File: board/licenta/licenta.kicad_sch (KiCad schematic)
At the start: 57 parts, among them IC1 SAMACSYS_PARTS_NCP186BMX330TAG, IC3 SAMACSYS_PARTS_BMI085, J1 SAMACSYS_PARTS_USB4110-GF-A, J2 SAMACSYS_PARTS_112A-TAAR-R03_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, Q1 ESP32_WROVER_SPARKFUN-DISCRET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, Q2 2N7002, SW1 SW_Push, SW2 SW_Push, SW3 SW_Push, SW6 SW_Push, U2 ESP32_WROVER_SPARKFUN-IC-POWE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, U3 DRV2605LDGS, U4 GC9A01_IPS_display_SPI, U7 ESP32-S3-MINI-1

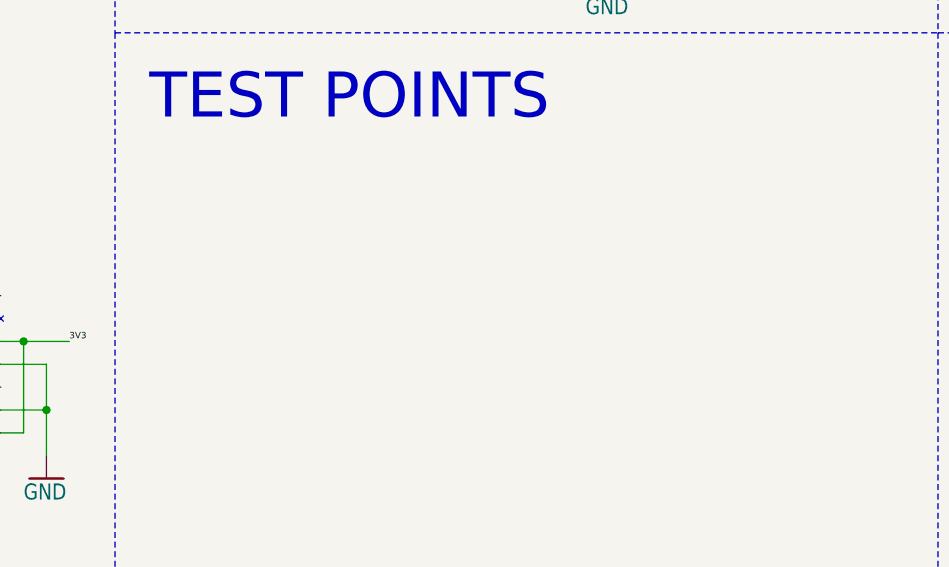
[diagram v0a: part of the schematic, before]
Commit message: Add DRU and minor pads update
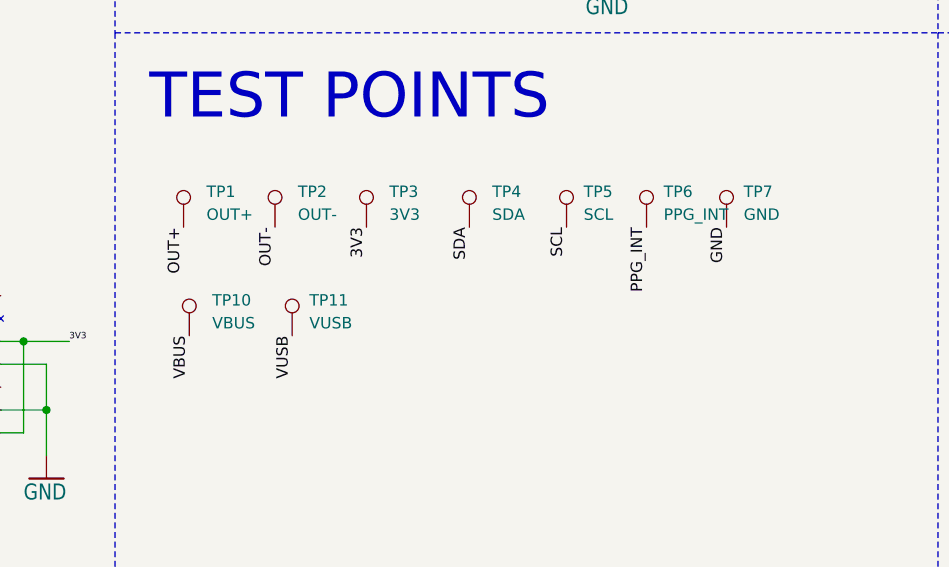
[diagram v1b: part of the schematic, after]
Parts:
- added TP1: OUT+, TestPoint:TestPoint_Pad_D2.0mm, symbol Connector:TestPoint
- added TP10: VBUS, TestPoint:TestPoint_Pad_1.0x1.0mm, symbol Connector:TestPoint
- added TP11: VUSB, TestPoint:TestPoint_Pad_1.0x1.0mm, symbol Connector:TestPoint
- added TP2: OUT-, TestPoint:TestPoint_Pad_D2.0mm, symbol Connector:TestPoint
- added TP3: 3V3, TestPoint:TestPoint_Pad_D2.0mm, symbol Connector:TestPoint
- added TP4: SDA, TestPoint:TestPoint_Pad_D2.0mm, symbol Connector:TestPoint
- added TP5: SCL, TestPoint:TestPoint_Pad_D2.0mm, symbol Connector:TestPoint
- added TP6: PPG_INT, TestPoint:TestPoint_Pad_D2.0mm, symbol Connector:TestPoint
- added TP7: GND, TestPoint:TestPoint_Pad_D2.0mm, symbol Connector:TestPoint
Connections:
- net 3V3: now also TP3.1
- net GND: now also TP7.1
- net OUT+: now also TP1.1
- net OUT-: now also TP2.1
- net PPG_INT: now also TP6.1
- net SCL: now also TP5.1
- net SDA: now also TP4.1
- net VBUS: now also TP10.1
- net VUSB: now also TP11.1

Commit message: Add DRC and start routing
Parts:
- removed TP11: VUSB, TestPoint:TestPoint_Pad_1.0x1.0mm, symbol Connector:TestPoint
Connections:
- net LTR_INT is gone; now on net IMU_INT: U7.15 (GPIO11/TOUCH11/ADC2_CH0/FSPID/FSPIIO5/SUBSPID)
- net DISP_RST: now also U7.20 (GPIO16/U0CTS/ADC2_CH5/XTAL_32K_N); no longer U7.10 (GPIO6/TOUCH6/ADC1_CH5)
- net GND: now also U7.1 (GND), U7.2 (GND), U7.42 (GND), U7.43 (GND), U7.46 (GND), U7.47 (GND), U7.48 (GND), U7.49 (GND), U7.50 (GND), U7.51 (GND), U7.52 (GND), U7.53 (GND), U7.54 (GND), U7.55 (GND), U7.56 (GND), U7.57 (GND), U7.58 (GND), U7.59 (GND), U7.60 (GND), U7.61 (GND), U7.62 (GND), U7.63 (GND), U7.64 (GND), U7.65 (GND)
- net IMU_INT: no longer U7.11 (GPIO7/TOUCH7/ADC1_CH6)
- net SS_SD: now also U7.21 (GPIO17/U1TXD/ADC2_CH6); no longer U7.9 (GPIO5/TOUCH5/ADC1_CH4)
- net TFT_DC: now also U7.22 (GPIO18/U1RXD/ADC2_CH7/CLK_OUT3); no longer U7.6 (GPIO2/TOUCH2/ADC1_CH1)
- net RX: no longer names the net of U7.36 (MTDO/GPIO40/CLK_OUT2)
- net TX: no longer names the net of U7.35 (MTCK/GPIO39/CLK_OUT3/SUBSPICS1)
- no-connect marks 1 -> 30
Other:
- moved on the sheet: C1_BAT0, C1_BAT2, C1_BAT3, C1_DRV1, C1_DRV2, C2, C3, C4, C5, C7, CHG_LED0, IC3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

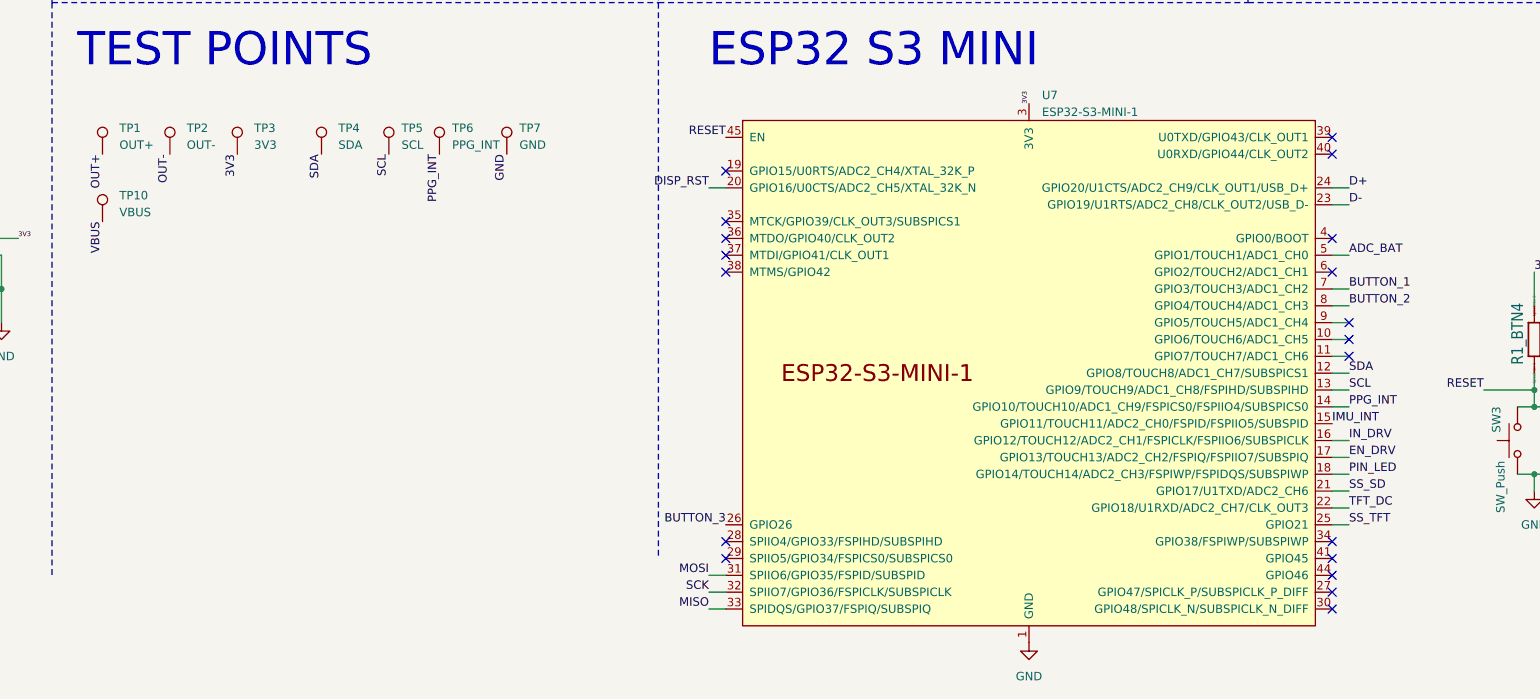
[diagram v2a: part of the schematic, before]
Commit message: Update PCB design
This commit changes the button footprints and modifies the silkscreen
of the PCB.
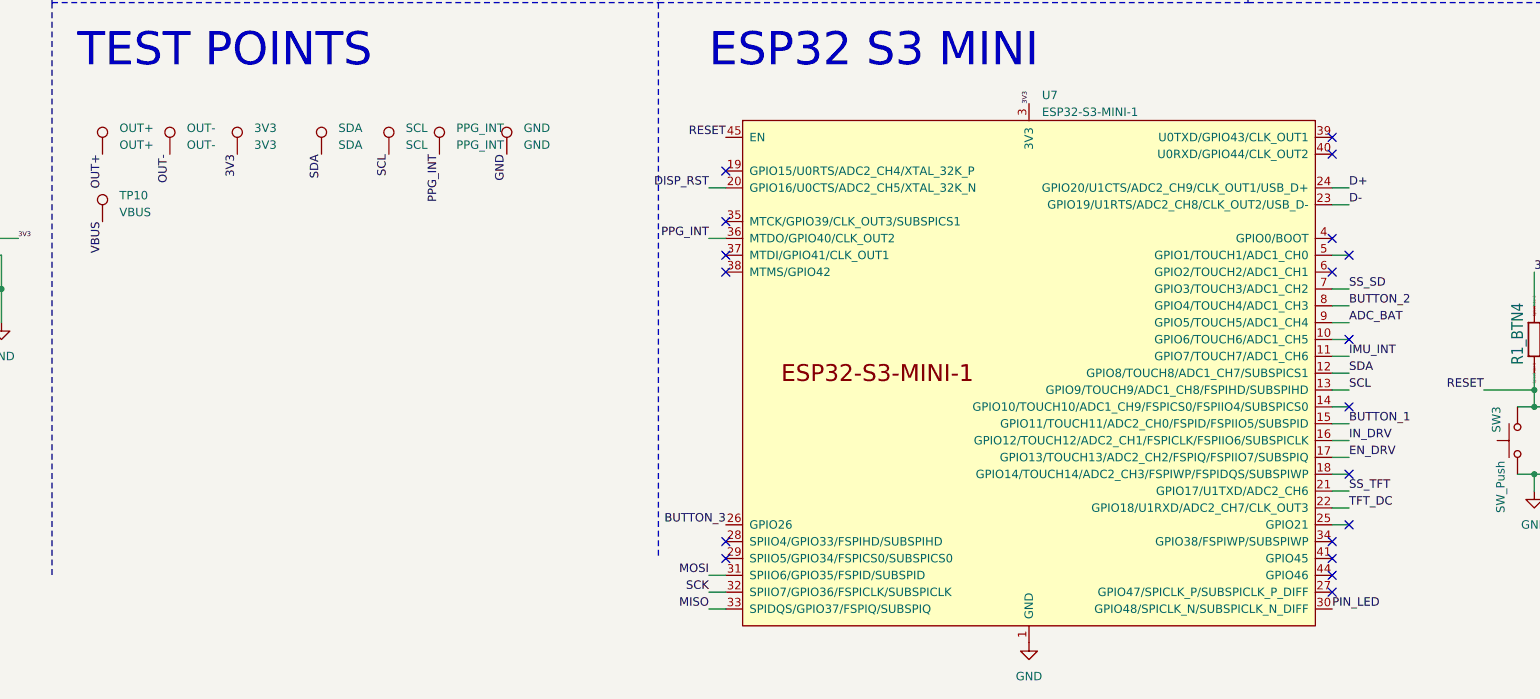
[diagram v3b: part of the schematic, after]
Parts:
- SW1, SW2, SW3, SW6: footprint open-Smartwatch:button_side_smd -> HW_licenta:EVQ-P7K01P
- renumbered TP3 to 3V3, TP7 to GND, TP1 to OUT+, TP2 to OUT-, TP6 to PPG_INT, TP5 to SCL, TP4 to SDA
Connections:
- net ADC_BAT: now also U7.9 (GPIO5/TOUCH5/ADC1_CH4); no longer U7.5 (GPIO1/TOUCH1/ADC1_CH0)
- net BUTTON_1: now also U7.15 (GPIO11/TOUCH11/ADC2_CH0/FSPID/FSPIIO5/SUBSPID); no longer U7.7 (GPIO3/TOUCH3/ADC1_CH2)
- net IMU_INT: now also U7.11 (GPIO7/TOUCH7/ADC1_CH6); no longer U7.15 (GPIO11/TOUCH11/ADC2_CH0/FSPID/FSPIIO5/SUBSPID)
- net PIN_LED: now also U7.30 (GPIO48/SPICLK_N/SUBSPICLK_N_DIFF); no longer U7.18 (GPIO14/TOUCH14/ADC2_CH3/FSPIWP/FSPIDQS/SUBSPIWP)
- net PPG_INT: now also U7.36 (MTDO/GPIO40/CLK_OUT2); no longer U7.14 (GPIO10/TOUCH10/ADC1_CH9/FSPICS0/FSPIIO4/SUBSPICS0)
- net SS_SD: now also U7.7 (GPIO3/TOUCH3/ADC1_CH2); no longer U7.21 (GPIO17/U1TXD/ADC2_CH6)
- net SS_TFT: now also U7.21 (GPIO17/U1TXD/ADC2_CH6); no longer U7.25 (GPIO21)

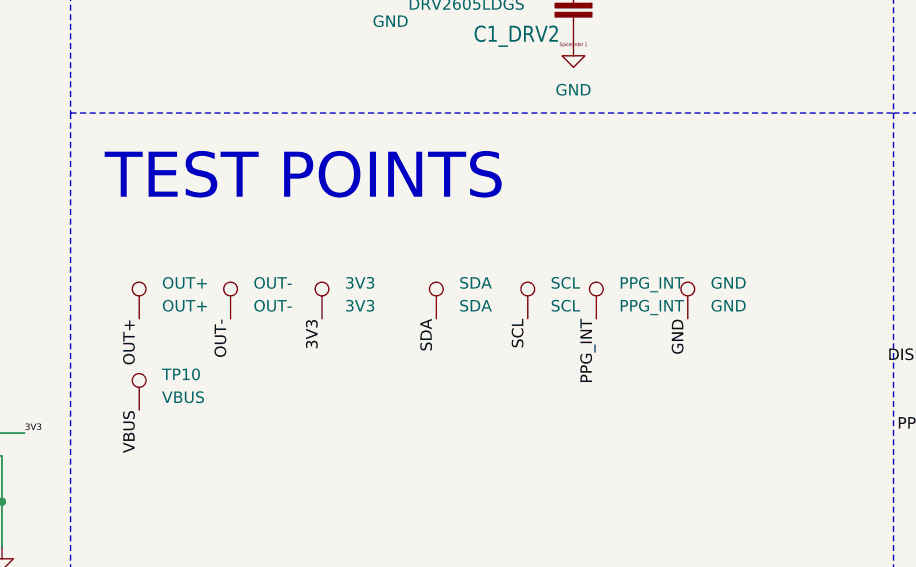
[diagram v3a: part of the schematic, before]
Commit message: Modify button alignment
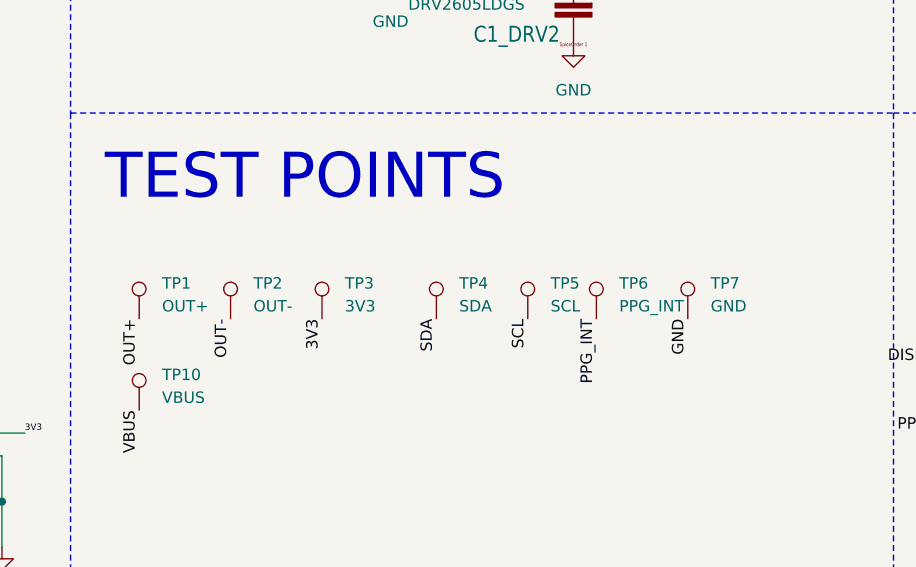
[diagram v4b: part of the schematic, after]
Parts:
- renumbered OUT+ to TP1, OUT- to TP2, 3V3 to TP3, SDA to TP4, SCL to TP5, PPG_INT to TP6, GND to TP7
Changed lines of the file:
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@@
   (symbol (lib_id "Connector:TestPoint") (at 154.94 213.36 0) (unit 1)
     (in_bom yes) (on_board yes) (dnp no) (fields_autoplaced)
-    (property "Reference" "GND" (at 157.48 209.423 0)
+    (property "Reference" "TP7" (at 157.48 209.423 0)
       (effects (font (size 1.27 1.27)) (justify left))
     )
@@
       (project "licenta"
         (path "/cd4c7fd1-8f21-4516-b6aa-ac99dec1dc72"
-          (reference "GND") (unit 1)
+          (reference "TP7") (unit 1)
         )
       )
@@
   (symbol (lib_id "Connector:TestPoint") (at 104.14 213.36 0) (unit 1)
     (in_bom yes) (on_board yes) (dnp no) (fields_autoplaced)
-    (property "Reference" "OUT-" (at 106.68 209.423 0)
+    (property "Reference" "TP2" (at 106.68 209.423 0)
       (effects (font (size 1.27 1.27)) (justify left))
     )
@@
       (project "licenta"
         (path "/cd4c7fd1-8f21-4516-b6aa-ac99dec1dc72"
-          (reference "OUT-") (unit 1)
+          (reference "TP2") (unit 1)
         )
       )
@@
   (symbol (lib_id "Connector:TestPoint") (at 127 213.36 0) (unit 1)
     (in_bom yes) (on_board yes) (dnp no) (fields_autoplaced)
-    (property "Reference" "SDA" (at 129.54 209.423 0)
+    (property "Reference" "TP4" (at 129.54 209.423 0)
       (effects (font (size 1.27 1.27)) (justify left))
     )
@@
       (project "licenta"
         (path "/cd4c7fd1-8f21-4516-b6aa-ac99dec1dc72"
-          (reference "SDA") (unit 1)
+          (reference "TP4") (unit 1)
         )
       )
@@
   (symbol (lib_id "Connector:TestPoint") (at 137.16 213.36 0) (unit 1)
     (in_bom yes) (on_board yes) (dnp no) (fields_autoplaced)
-    (property "Reference" "SCL" (at 139.7 209.423 0)
+    (property "Reference" "TP5" (at 139.7 209.423 0)
       (effects (font (size 1.27 1.27)) (justify left))
     )
@@
       (project "licenta"
         (path "/cd4c7fd1-8f21-4516-b6aa-ac99dec1dc72"
-          (reference "SCL") (unit 1)
+          (reference "TP5") (unit 1)
         )
       )
@@
   (symbol (lib_id "Connector:TestPoint") (at 144.78 213.36 0) (unit 1)
     (in_bom yes) (on_board yes) (dnp no) (fields_autoplaced)
-    (property "Reference" "PPG_INT" (at 147.32 209.423 0)
+    (property "Reference" "TP6" (at 147.32 209.423 0)
       (effects (font (size 1.27 1.27)) (justify left))
     )
@@
       (project "licenta"
         (path "/cd4c7fd1-8f21-4516-b6aa-ac99dec1dc72"
-          (reference "PPG_INT") (unit 1)
+          (reference "TP6") (unit 1)
         )
       )
@@
   (symbol (lib_id "Connector:TestPoint") (at 93.98 213.36 0) (unit 1)
     (in_bom yes) (on_board yes) (dnp no) (fields_autoplaced)
-    (property "Reference" "OUT+" (at 96.52 209.423 0)
+    (property "Reference" "TP1" (at 96.52 209.423 0)
       (effects (font (size 1.27 1.27)) (justify left))
     )
@@
       (project "licenta"
         (path "/cd4c7fd1-8f21-4516-b6aa-ac99dec1dc72"
-          (reference "OUT+") (unit 1)
+          (reference "TP1") (unit 1)
         )
       )
@@
   (symbol (lib_id "Connector:TestPoint") (at 114.3 213.36 0) (unit 1)
     (in_bom yes) (on_board yes) (dnp no) (fields_autoplaced)
-    (property "Reference" "3V3" (at 116.84 209.423 0)
+    (property "Reference" "TP3" (at 116.84 209.423 0)
       (effects (font (size 1.27 1.27)) (justify left))
     )
@@
       (project "licenta"
         (path "/cd4c7fd1-8f21-4516-b6aa-ac99dec1dc72"
-          (reference "3V3") (unit 1)
-        )
-      )
+          (reference "TP3") (unit 1)
+        )
+      )

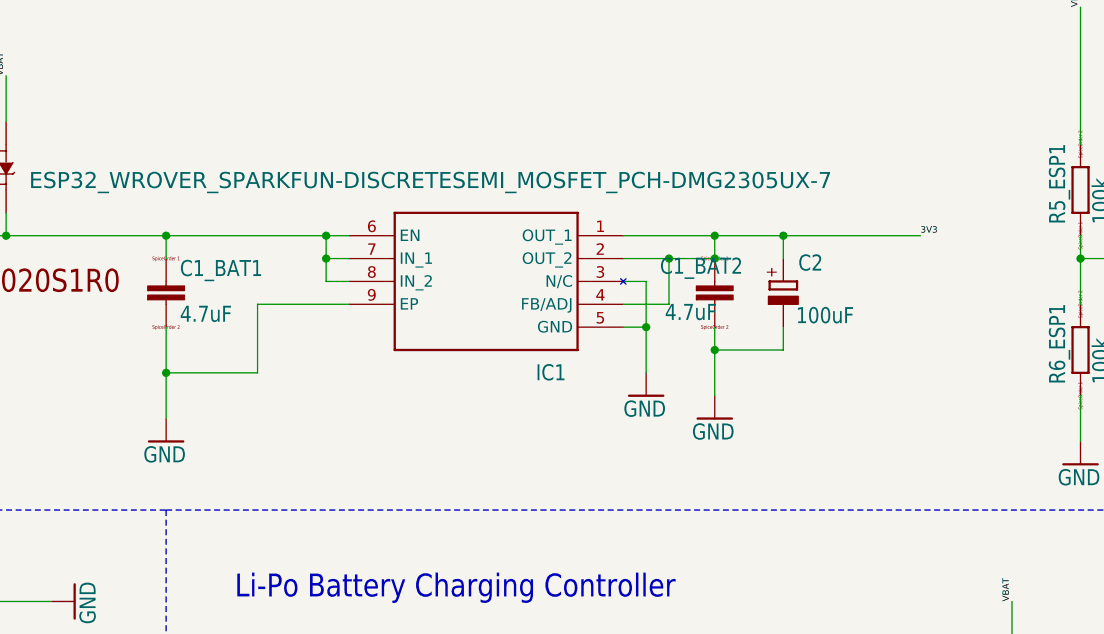
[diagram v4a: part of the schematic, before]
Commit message: Update PCB and schematics
This commit replaces the LDO and imports new libraries
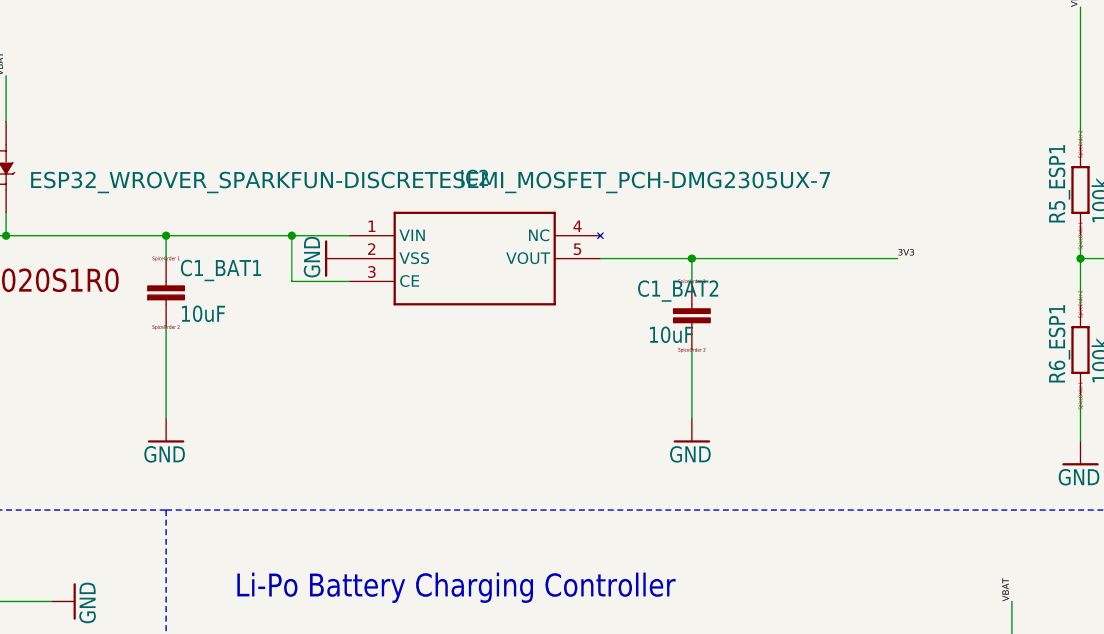
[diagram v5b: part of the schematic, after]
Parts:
- removed C2: 100uF, mini_iot:RCL_CT3528, symbol mini_iot-eagle-import:RCL_CPOL-EUCT3528
- removed IC1: SAMACSYS_PARTS_NCP186BMX330TAG, mini_iot:SAMACSYS_PARTS_NCP186AMX330TAG, symbol mini_iot-eagle-import:SAMACSYS_PARTS_NCP186BMX330TAG
- added IC2: ~, mini_iot:XC8107AC20MR-G, symbol mini-iot-NEW:XC6220A331MR-G
- C1_BAT1, C1_BAT2: value 4.7uF -> 10uF
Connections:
- net 3V3: now also IC2.5 (VOUT)
- net GND: now also IC2.2 (VSS)
- net at C1_BAT1.1, D2.1 (CATHODE), Q1.2 (S): now also IC2.1 (VIN), IC2.3 (CE)
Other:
- moved on the sheet: C1_BAT2

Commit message: Update board and schematic
This commit adds the following modifications:
- SDA and SCL pull-ups
- 100nF debounce capacitors for buttons
- vias tweaks to not come out of pads
- connect one button to be used both as BOOT and GPIO
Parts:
- added R_SCL1, R_SDA1: 4k7, mini_iot:ESP32_WROVER_EAGLE-LTSPICE_R0402, symbol mini_iot-eagle-import:ESP32_WROVER_EAGLE-LTSPICE_RR0402
- C3, C4, C5, C7: value 1uF -> 100nF
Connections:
- net BUTTON_3 is gone; now on net BUTTON_2: C5.2, R1_BTN2.1, SW2.2, U7.26 (GPIO26)
- net 3V3: now also R_SCL1.2, R_SDA1.2
- net BUTTON_2: no longer C4.2, R1_BTN1.1, SW1.2, U7.8 (GPIO4/TOUCH4/ADC1_CH3)
- net SCL: now also R_SCL1.1
- net SDA: now also R_SDA1.1
- net BOOT: now reaches U7.4 (GPIO0/BOOT)
- net BOOT: now also C4.2, R1_BTN1.1, SW1.2

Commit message: Update schematic appearance
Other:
- note added: "I2C pull-ups"
- title: (none) -> Proiect TSC
- moved on the sheet: C1_BAT0, C1_BAT1, C1_BAT2, C2_BAT0, C7, CHG_LED0, D2, IC2, IC3, R1_BAT0, R1_BTN4, R1_PWRBUS0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
